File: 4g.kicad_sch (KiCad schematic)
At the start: 18 parts, among them J3 SIM7600X-M2-B, J6 SIM8066-6-1-14-01-A

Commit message: Schematic Done
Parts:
- added C26: C_100n_0402, jetson-orin-baseboard-footprints:0402-cap, symbol jetson-orin-baseboard:C_100n_0402
- added C49: C_10u_0402, jetson-orin-baseboard-footprints:0402-cap, symbol jetson-orin-baseboard:C_10u_0402
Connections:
- net +3.3V is gone; now on net +3V3: J3.2 (3.3V), J3.4 (3.3V), J3.70 (3.3V), J3.72 (3.3V), J3.74 (3.3V)
- net +3V3: now also C26.1, C49.1
- net GND: now also C26.2, C49.2
- net USB2_D_N: now also R32.1; no longer R31.1
- net USB2_D_P: now also R31.1; no longer R32.1
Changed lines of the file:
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@@
   (junction (at 133.35 112.395) (diameter 0) (color 0 0 0 0)
   )
+  (junction (at 183.515 57.785) (diameter 0) (color 0 0 0 0)
+  )
   (junction (at 140.97 122.555) (diameter 0) (color 0 0 0 0)
   )
   (junction (at 138.43 120.015) (diameter 0) (color 0 0 0 0)
   )
+  (junction (at 194.945 50.165) (diameter 0) (color 0 0 0 0)
+  )
   (junction (at 73.025 117.475) (diameter 0) (color 0 0 0 0)
   )
@@
   )
   (junction (at 274.955 149.86) (diameter 0) (color 0 0 0 0)
+  )
+  (junction (at 187.325 50.165) (diameter 0) (color 0 0 0 0)
   )
   (junction (at 119.38 125.095) (diameter 0) (color 0 0 0 0)
@@
     (stroke (width 0) (type default))
   )
+  (wire (pts (xy 179.705 57.785) (xy 183.515 57.785))
+    (stroke (width 0) (type default))
+  )
   (wire (pts (xy 96.52 135.89) (xy 96.52 137.16))
     (stroke (width 0) (type default))
@@
     (stroke (width 0) (type default))
   )
+  (wire (pts (xy 179.705 50.165) (xy 187.325 50.165))
+    (stroke (width 0) (type default))
+  )
   (wire (pts (xy 61.595 112.395) (xy 80.01 112.395))
     (stroke (width 0) (type default))
@@
     (stroke (width 0) (type default))
   )
+  (wire (pts (xy 194.945 50.165) (xy 194.945 45.085))
+    (stroke (width 0) (type default))
+  )
   (wire (pts (xy 162.56 60.325) (xy 162.56 61.595))
     (stroke (width 0) (type default))
@@
     (stroke (width 0) (type default))
   )
+  (wire (pts (xy 194.945 50.165) (xy 194.945 61.595))
+    (stroke (width 0) (type default))
+  )
   (wire (pts (xy 220.345 71.755) (xy 225.425 71.755))
     (stroke (width 0) (type default))
@@
     (stroke (width 0) (type default))
   )
+  (wire (pts (xy 183.515 57.785) (xy 187.325 57.785))
+    (stroke (width 0) (type default))
+  )
   (wire (pts (xy 259.08 149.86) (xy 261.62 149.86))
     (stroke (width 0) (type default))
@@
     (stroke (width 0) (type default))
   )
+  (wire (pts (xy 187.325 50.165) (xy 194.945 50.165))
+    (stroke (width 0) (type default))
+  )
   (wire (pts (xy 274.955 149.86) (xy 271.78 149.86))
     (stroke (width 0) (type default))
@@
   )
   (wire (pts (xy 87.63 120.015) (xy 96.52 120.015))
-    (stroke (width 0) (type default))
-  )
-  (wire (pts (xy 194.945 59.055) (xy 194.945 61.595))
     (stroke (width 0) (type default))
   )
@@
     (effects (font (size 4 4) (thickness 0.5994) bold) (justify left bottom))
   )
-  (global_label "USB2_D_N" (shape input) (at 145.415 77.47 180)
+  (global_label "USB2_D_N" (shape input) (at 145.415 80.01 180)
     (effects (font (size 1.27 1.27)) (justify right))
-    (property "Intersheetrefs" "${INTERSHEET_REFS}" (at 129.54 77.47 0)
+    (property "Intersheetrefs" "${INTERSHEET_REFS}" (at 129.54 80.01 0)
       (effects (font (size 1.1 1.1)) (justify right))
     )
@@
     )
   )
-  (global_label "USB2_D_P" (shape input) (at 145.415 80.01 180)
+  (global_label "USB2_D_P" (shape input) (at 145.415 77.47 180)
     (effects (font (size 1.27 1.27)) (justify right))
-    (property "Intersheetrefs" "${INTERSHEET_REFS}" (at 129.54 80.01 0)
+    (property "Intersheetrefs" "${INTERSHEET_REFS}" (at 129.54 77.47 0)
       (effects (font (size 1.1 1.1)) (justify right))
     )
@@
       (effects (font (size 1.27 1.27)) hide)
     )
-    (property "Datasheet" "http://read.pudn.com/downloads794/doc/project/3133918/PCIe_M.2_Electromechanical_Spec_Rev1.0_Final_11012013_RS_Clean.pdf#page=154" (at 194.945 165.735 0)
+    (property "Datasheet" "https://files.waveshare.com/upload/0/02/SIM7600X-M2_Hardware_Design_V1.01.pdf" (at 194.945 165.735 0)
       (effects (font (size 1.27 1.27)) hide)
     )
@@
     )
   )
-  (symbol (lib_id "power:+3.3V") (at 194.945 59.055 0) (unit 1)
-    (in_bom yes) (on_board yes) (dnp no) (fields_autoplaced)
-    (property "Reference" "#PWR031" (at 194.945 62.865 0)
-      (effects (font (size 1.27 1.27)) hide)
-    )
-    (property "Value" "+3.3V" (at 194.945 53.975 0)
-      (effects (font (size 1.27 1.27)))
-    )
-    (property "Footprint" "" (at 194.945 59.055 0)
-      (effects (font (size 1.27 1.27)) hide)
-    )
-    (property "Datasheet" "" (at 194.945 59.055 0)
-      (effects (font (size 1.27 1.27)) hide)
-    )
-    (pin "1")
-    (instances
-      (project "jetson-orin-baseboard"
-        (path "/4b393452-b11e-416e-bc83-918ae3cab2f1/2fa436cd-5c26-4e4a-b48c-59983497db7a"
-          (reference "#PWR031") (unit 1)
-        )
-      )
-    )
-  )
   (symbol (lib_id "power:GND") (at 225.425 71.755 0) (unit 1)
     (in_bom yes) (on_board yes) (dnp no) (fields_autoplaced)
@@
         (path "/4b393452-b11e-416e-bc83-918ae3cab2f1/2fa436cd-5c26-4e4a-b48c-59983497db7a"
           (reference "#PWR030") (unit 1)
+        )
+      )
+    )
+  )
+  (symbol (lib_id "jetson-orin-baseboard:C_100n_0402") (at 187.325 53.975 0) (unit 1)
+    (in_bom yes) (on_board yes) (dnp no)
+    (property "Reference" "C26" (at 191.77 51.435 0)
+      (effects (font (size 1.27 1.27)) (justify right))
+    )
+    (property "Value" "C_100n_0402" (at 187.325 57.785 0)
+      (effects (font (size 1.27 1.27)) hide)
+    )
+    (property "Footprint" "jetson-orin-baseboard-footprints:0402-cap" (at 192.405 48.895 0)
+      (effects (font (size 1.524 1.524)) (justify left) hide)
+    )
+    (property "Datasheet" "" (at 187.325 53.975 0)
+      (effects (font (size 1.27 1.27)) hide)
+    )
+    (property "Manufacturer" "Murata" (at 192.405 43.815 0)
+      (effects (font (size 1.524 1.524)) (justify left) hide)
+    )
+    (property "MPN" "GRM155R61H104KE14D" (at 192.405 46.355 0)
+      (effects (font (size 1.524 1.524)) (justify left) hide)
+    )
+    (property "Val" "100n" (at 192.405 56.515 0)
+      (effects (font (size 1.27 1.27)) (justify right))
+    )
+    (pin "1")
+    (pin "2")
+    (instances
+      (project "jetson-orin-baseboard"
+        (path "/4b393452-b11e-416e-bc83-918ae3cab2f1/ea236701-ba50-4026-b890-5436b3eb8139"
+          (reference "C26") (unit 1)
+        )
+        (path "/4b393452-b11e-416e-bc83-918ae3cab2f1/2fa436cd-5c26-4e4a-b48c-59983497db7a"
+          (reference "C90") (unit 1)
         )
       )
@@
     )
   )
+  (symbol (lib_id "power:GND") (at 183.515 57.785 0) (unit 1)
+    (in_bom yes) (on_board yes) (dnp no) (fields_autoplaced)
+    (property "Reference" "#PWR031" (at 183.515 64.135 0)
+      (effects (font (size 1.27 1.27)) hide)
+    )
+    (property "Value" "GND" (at 183.515 62.23 0)
+      (effects (font (size 1.27 1.27)))
+    )
+    (property "Footprint" "" (at 183.515 57.785 0)
+      (effects (font (size 1.27 1.27)) hide)
+    )
+    (property "Datasheet" "" (at 183.515 57.785 0)
+      (effects (font (size 1.27 1.27)) hide)
+    )
+    (pin "1")
+    (instances
+      (project "jetson-orin-baseboard"
+        (path "/4b393452-b11e-416e-bc83-918ae3cab2f1/2fa436cd-5c26-4e4a-b48c-59983497db7a"
+          (reference "#PWR031") (unit 1)
+        )
+      )
+    )
+  )
   (symbol (lib_id "jetson-orin-baseboard:TPD1E0B04DPYR ") (at 266.7 139.7 0) (unit 1)
     (in_bom yes) (on_board yes) (dnp no) (fields_autoplaced)
@@
         (path "/4b393452-b11e-416e-bc83-918ae3cab2f1/2fa436cd-5c26-4e4a-b48c-59983497db7a"
           (reference "C35") (unit 1)
+        )
+      )
+    )
+  )
+  (symbol (lib_id "jetson-orin-baseboard:+3V3") (at 194.945 45.085 0) (unit 1)
+    (in_bom yes) (on_board yes) (dnp no)
+    (property "Reference" "#PWR0230" (at 194.945 48.895 0)
+      (effects (font (size 1.27 1.27)) hide)
+    )
+    (property "Value" "+3V3" (at 194.945 41.275 0)
+      (effects (font (size 1.27 1.27)))
+    )
+    (property "Footprint" "" (at 194.945 45.085 0)
+      (effects (font (size 1.27 1.27)) hide)
+    )
+    (property "Datasheet" "" (at 194.945 45.085 0)
+      (effects (font (size 1.27 1.27)) hide)
+    )
+    (pin "1")
+    (instances
+      (project "jetson-orin-baseboard"
+        (path "/4b393452-b11e-416e-bc83-918ae3cab2f1/e2c0f9a7-dbaa-401b-8614-57eda30161fa"
+          (reference "#PWR0230") (unit 1)
+        )
+        (path "/4b393452-b11e-416e-bc83-918ae3cab2f1/2fa436cd-5c26-4e4a-b48c-59983497db7a"
+          (reference "#PWR024") (unit 1)
         )
       )
@@
         )
       )
+    )
+  )
+  (symbol (lib_id "jetson-orin-baseboard:C_10u_0402") (at 179.705 53.975 0) (unit 1)
+    (in_bom yes) (on_board yes) (dnp no)
+    (property "Reference" "C49" (at 180.34 51.435 0)
+      (effects (font (size 1.27 1.27)) (justify left))
+    )
+    (property "Value" "C_10u_0402" (at 179.705 57.785 0)
+      (effects (font (size 1.27 1.27)) hide)
+    )
+    (property "Footprint" "jetson-orin-baseboard-footprints:0402-cap" (at 184.785 48.895 0)
+      (effects (font (size 1.524 1.524)) (justify left) hide)
+    )
+    (property "Datasheet" "" (at 179.705 53.975 0)
+      (effects (font (size 1.27 1.27)) hide)
+    )
+    (property "Manufacturer" "YAGEO" (at 184.785 43.815 0)
+      (effects (font (size 1.524 1.524)) (justify left) hide)
+    )
+    (property "MPN" "CC0402MRX5R5BB106" (at 184.785 46.355 0)
+      (effects (font (size 1.524 1.524)) (justify left) hide)
+    )
+    (property "Val" "10u" (at 180.975 56.515 0)
+      (effects (font (size 1.27 1.27)) (justify left))
+    )
+    (pin "1")
+    (pin "2")
+    (instances
+      (project "jetson-orin-baseboard"
+        (path "/4b393452-b11e-416e-bc83-918ae3cab2f1/ea236701-ba50-4026-b890-5436b3eb8139"
+          (reference "C49") (unit 1)
+        )
+        (path "/4b393452-b11e-416e-bc83-918ae3cab2f1/2fa436cd-5c26-4e4a-b48c-59983497db7a"
+          (reference "C89") (unit 1)
+        )
+      )

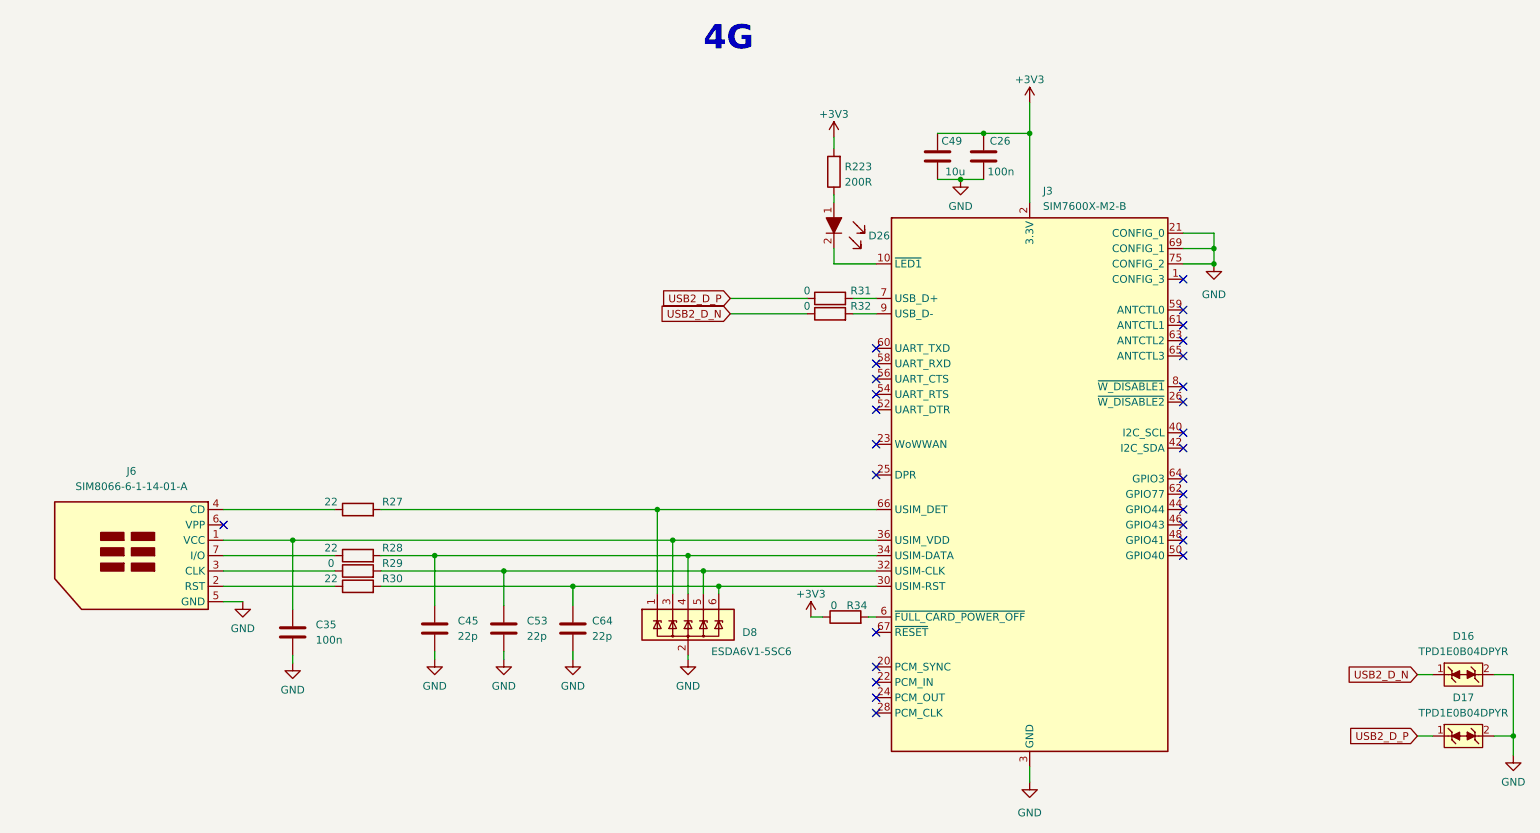
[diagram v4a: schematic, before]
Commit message: Schematic V1 and footprints assigned
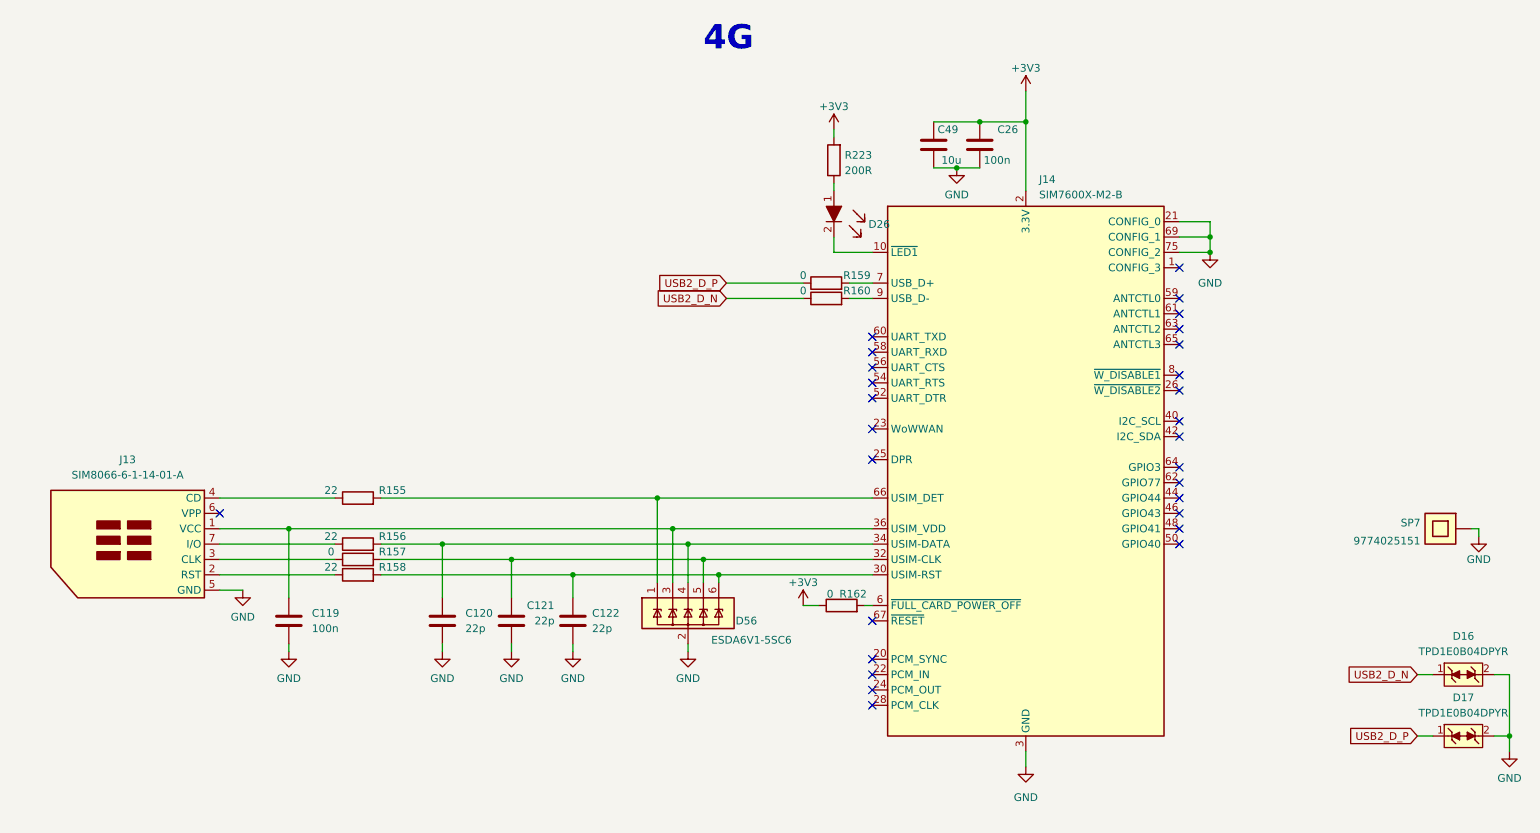
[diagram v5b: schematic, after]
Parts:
- added SP7: 9774025151, jetson-orin-baseboard-footprints:9774025151, symbol jetson-orin-baseboard:9774025151
- C119: renamed from C35; footprint (none) -> jetson-orin-baseboard-footprints:0402-cap
- C120: renamed from C45; footprint (none) -> jetson-orin-baseboard-footprints:0402-cap
- C121: renamed from C53; footprint (none) -> jetson-orin-baseboard-footprints:0402-cap
- C122: renamed from C64; footprint (none) -> jetson-orin-baseboard-footprints:0402-cap
- J13: renamed from J6; footprint (none) -> jetson-orin-baseboard-footprints:GCT_SIM8066-6-1-14-01-A_REVA
- J14: renamed from J3; footprint (none) -> jetson-orin-baseboard-footprints:TE_2199230-3
- R155: renamed from R27; footprint (none) -> jetson-orin-baseboard-footprints:0402-res
- R156: renamed from R28; footprint (none) -> jetson-orin-baseboard-footprints:0402-res
- R157: renamed from R29; footprint (none) -> jetson-orin-baseboard-footprints:0402-res
- R158: renamed from R30; footprint (none) -> jetson-orin-baseboard-footprints:0402-res
- R159: renamed from R31; footprint (none) -> jetson-orin-baseboard-footprints:0402-res
- R160: renamed from R32; footprint (none) -> jetson-orin-baseboard-footprints:0402-res
- R162: renamed from R34; footprint (none) -> jetson-orin-baseboard-footprints:0402-res
- renumbered D8 to D56
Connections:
- net GND: now also SP7.1
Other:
- moved on the sheet: C119, C120, C121, C122, C26, C49, D26, D56, J13, J14, R155, R156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

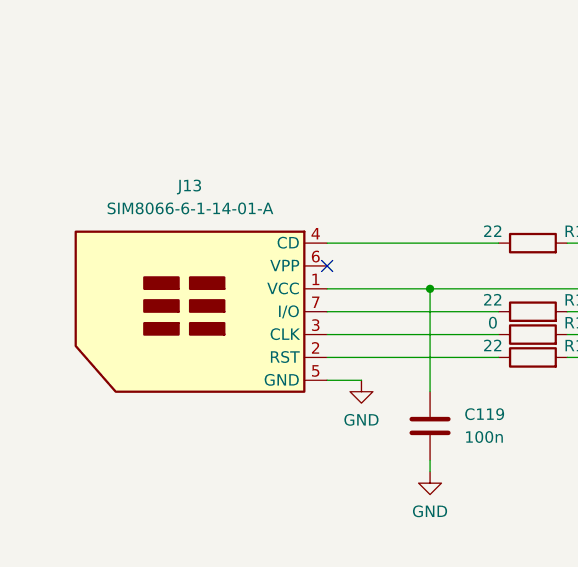
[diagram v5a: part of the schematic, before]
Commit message: Footprints well assigned, XT30 added, Shields grounded
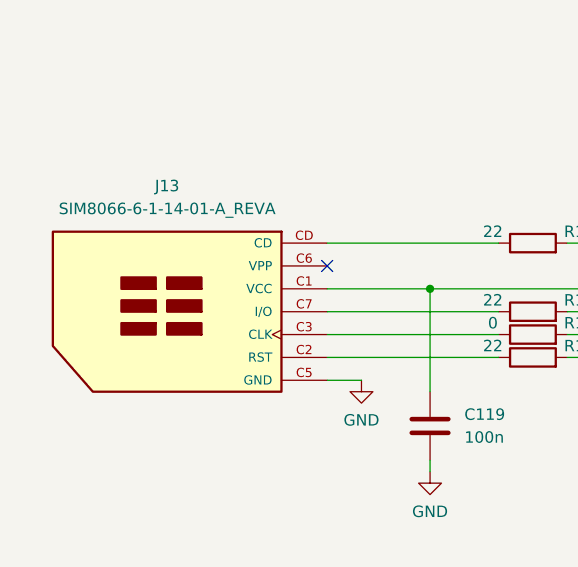
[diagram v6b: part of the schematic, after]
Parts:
- removed J13: SIM8066-6-1-14-01-A, jetson-orin-baseboard-footprints:GCT_SIM8066-6-1-14-01-A_REVA, symbol jetson-orin-baseboard:SIM_Card_With_Detect
- added J13: SIM8066-6-1-14-01-A_REVA, jetson-orin-baseboard-footprints:GCT_SIM8066-6-1-14-01-A_REVA, symbol SIM8066-6-1-14-01-A_REVA:SIM8066-6-1-14-01-A_REVA
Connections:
- net GND: now also J14.S1, J14.S2, J13.C5 (GND), J13.G1 (GND), J13.G2 (GND), J13.G3 (GND), J13.G4 (GND)
- net at C119.1, D56.3 (IO2), J14.36 (USIM_VDD): now also J13.C1 (VCC)
- net at R156.1: now also J13.C7 (I/O)
- net at R157.1: now also J13.C3 (CLK)
- net at R155.1: now also J13.CD
- net at R158.1: now also J13.C2 (RST)
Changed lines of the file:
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@@
     (pin "8")
     (pin "9")
+    (pin "S1")
+    (pin "S2")
     (instances
       (project "jetson-orin-baseboard"
@@
     )
   )
+  (symbol (lib_name "SIM8066-6-1-14-01-A_REVA_1") (lib_id "SIM8066-6-1-14-01-A_REVA:SIM8066-6-1-14-01-A_REVA") (at 50.8 118.11 0) (mirror y) (unit 1)
+    (in_bom yes) (on_board yes) (dnp no) (fields_autoplaced)
+    (property "Reference" "J13" (at 43.18 104.14 0)
+      (effects (font (size 1.27 1.27)))
+    )
+    (property "Value" "SIM8066-6-1-14-01-A_REVA" (at 43.18 106.68 0)
+      (effects (font (size 1.27 1.27)))
+    )
+    (property "Footprint" "jetson-orin-baseboard-footprints:GCT_SIM8066-6-1-14-01-A_REVA" (at 50.8 130.81 0)
+      (effects (font (size 1.27 1.27)) (justify bottom) hide)
+    )
+    (property "Datasheet" "" (at 50.8 130.81 0)
+      (effects (font (size 1.27 1.27)) hide)
+    )
+    (property "MF" "Global Connector Technology" (at 50.8 130.81 0)
+      (effects (font (size 1.27 1.27)) (justify bottom) hide)
+    )
+    (property "MAXIMUM_PACKAGE_HEIGHT" "1.44mm" (at 50.8 130.81 0)
+      (effects (font (size 1.27 1.27)) (justify bottom) hide)
+    )
+    (property "Package" "None" (at 50.8 130.81 0)
+      (effects (font (size 1.27 1.27)) (justify bottom) hide)
+    )
+    (property "Price" "None" (at 50.8 130.81 0)
+      (effects (font (size 1.27 1.27)) (justify bottom) hide)
+    )
+    (property "Check_prices" "https://www.snapeda.com/parts/SIM8066-6-1-14-01-A/Global+Connector+Technology/view-part/?ref=eda" (at 50.8 130.81 0)
+      (effects (font (size 1.27 1.27)) (justify bottom) hide)
+    )
+    (property "STANDARD" "Manufacturer recommendations" (at 50.8 130.81 0)
+      (effects (font (size 1.27 1.27)) (justify bottom) hide)
+    )
+    (property "PARTREV" "REVA" (at 50.8 130.81 0)
+      (effects (font (size 1.27 1.27)) (justify bottom) hide)
+    )
+    (property "SnapEDA_Link" "https://www.snapeda.com/parts/SIM8066-6-1-14-01-A/Global+Connector+Technology/view-part/?ref=snap" (at 50.8 130.81 0)
+      (effects (font (size 1.27 1.27)) (justify bottom) hide)
+    )
+    (property "MP" "SIM8066-6-1-14-01-A" (at 50.8 130.81 0)
+      (effects (font (size 1.27 1.27)) (justify bottom) hide)
+    )
+    (property "Description" "\n7 (6 + 1) Position Card Connector NANO SIM Surface Mount, Right Angle Gold\n" (at 50.8 130.81 0)
+      (effects (font (size 1.27 1.27)) (justify bottom) hide)
+    )
+    (property "Availability" "In Stock" (at 50.8 130.81 0)
+      (effects (font (size 1.27 1.27)) (justify bottom) hide)
+    )
+    (property "MANUFACTURER" "Global Connector Technology" (at 50.8 130.81 0)
+      (effects (font (size 1.27 1.27)) (justify bottom) hide)
+    )
+    (pin "C1")
+    (pin "C2")
+    (pin "C3")
+    (pin "C5")
+    (pin "C6")
+    (pin "C7")
+    (pin "CD")
+    (pin "G1")
+    (pin "G2")
+    (pin "G3")
+    (pin "G4")
+    (instances
+      (project "jetson-orin-baseboard"
+        (path "/4b393452-b11e-416e-bc83-918ae3cab2f1/2fa436cd-5c26-4e4a-b48c-59983497db7a"
+          (reference "J13") (unit 1)
+        )
+      )
+    )
+  )
   (symbol (lib_id "jetson-orin-baseboard:R_200R_0402") (at 162.56 54.61 90) (unit 1)
     (in_bom yes) (on_board yes) (dnp no) (fields_autoplaced)
@@
         )
       )
-    )
-  )
-  (symbol (lib_id "jetson-orin-baseboard:SIM_Card_With_Detect") (at 48.26 118.11 0) (mirror y) (unit 1)
-    (in_bom yes) (on_board yes) (dnp no) (fields_autoplaced)
-    (property "Reference" "J13" (at 45.72 104.14 0)
-      (effects (font (size 1.27 1.27)))
-    )
-    (property "Value" "SIM8066-6-1-14-01-A" (at 45.72 106.68 0)
-      (effects (font (size 1.27 1.27)))
-    )
-    (property "Footprint" "jetson-orin-baseboard-footprints:GCT_SIM8066-6-1-14-01-A_REVA" (at 48.26 109.22 0)
-      (effects (font (size 1.27 1.27)) hide)
-    )
-    (property "Datasheet" " ~" (at 49.53 118.11 0)
-      (effects (font (size 1.27 1.27)) hide)
-    )
-    (pin "1")
-    (pin "2")
-    (pin "3")
-    (pin "4")
-    (pin "5")
-    (pin "6")
-    (pin "7")
-    (instances
-      (project "jetson-orin-baseboard"
-        (path "/4b393452-b11e-416e-bc83-918ae3cab2f1/2fa436cd-5c26-4e4a-b48c-59983497db7a"
-          (reference "J13") (unit 1)
-        )
-      )
